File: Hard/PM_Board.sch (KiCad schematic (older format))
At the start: 66 parts, among them J1 Micro_SD_Card_Det_Hirose_DM3AT, J101 LiPo_V+, J102 LiPo_V-, J2 KRC_Conn_SWD, J3 USB_B_Micro, J4 KRC_Conn_CAN, J5 KRC_Conn_CAN, J6 Umbilical, Q1 SSM6J501NU, Q2 2n7002, U1 CY8C58xxLTI-LPxxx, U2 INA226, U3 NCV7342, Y1 24MHz

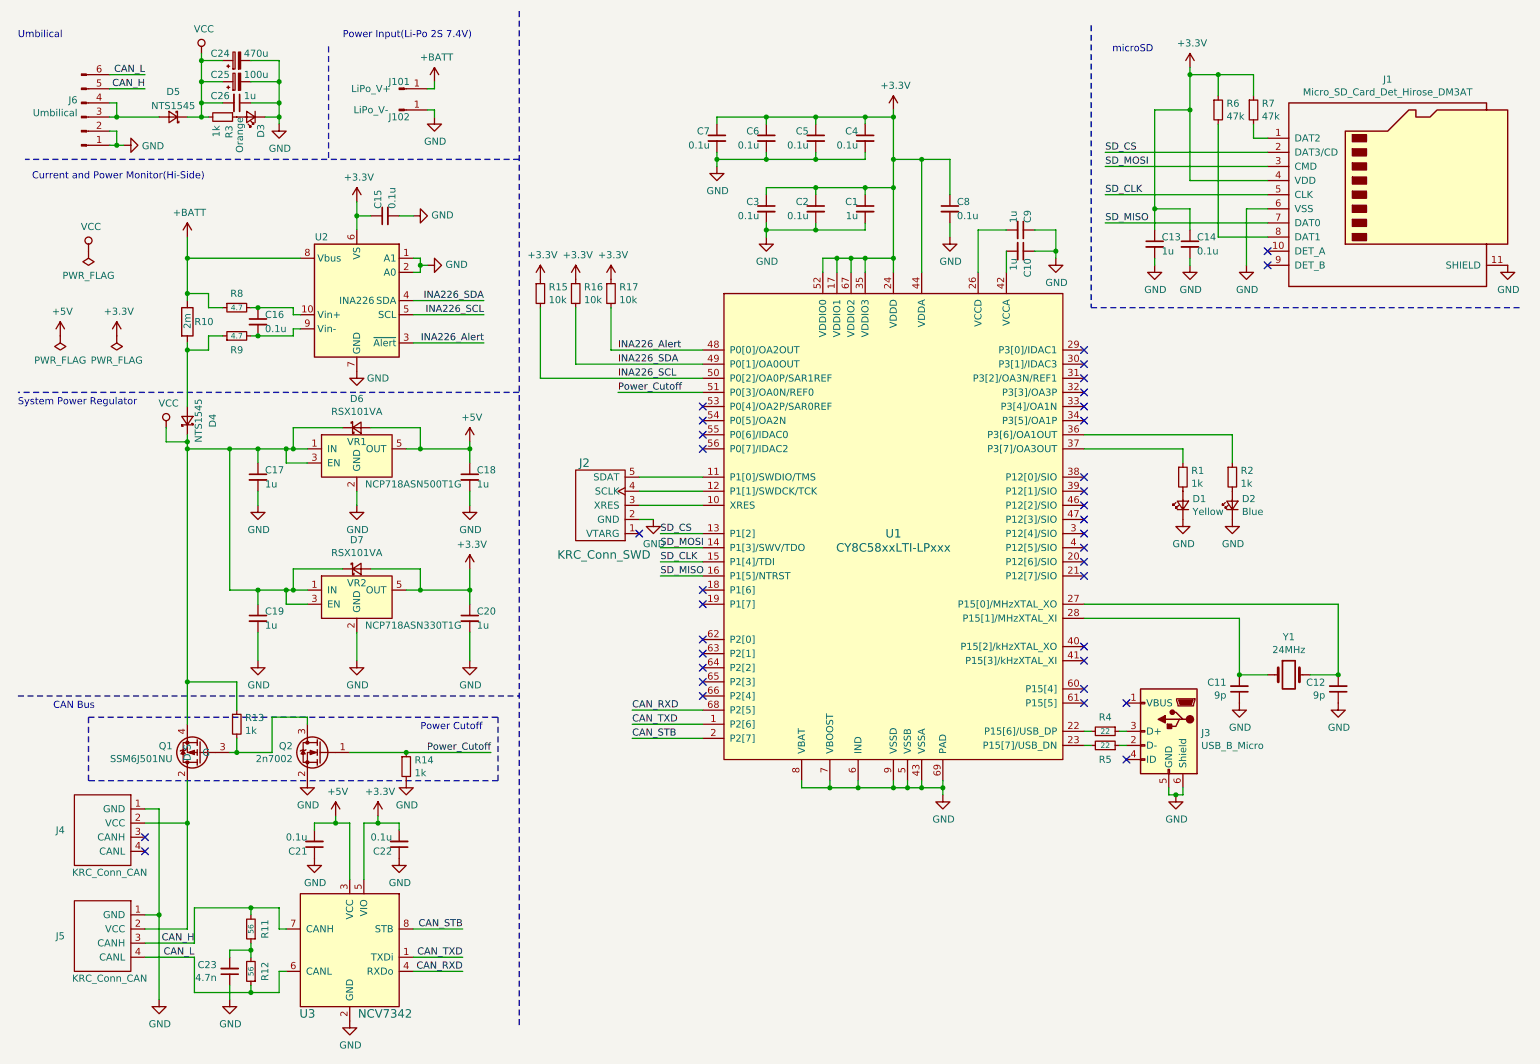
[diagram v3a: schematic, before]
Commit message: [update] SDカード用のLDOを追加
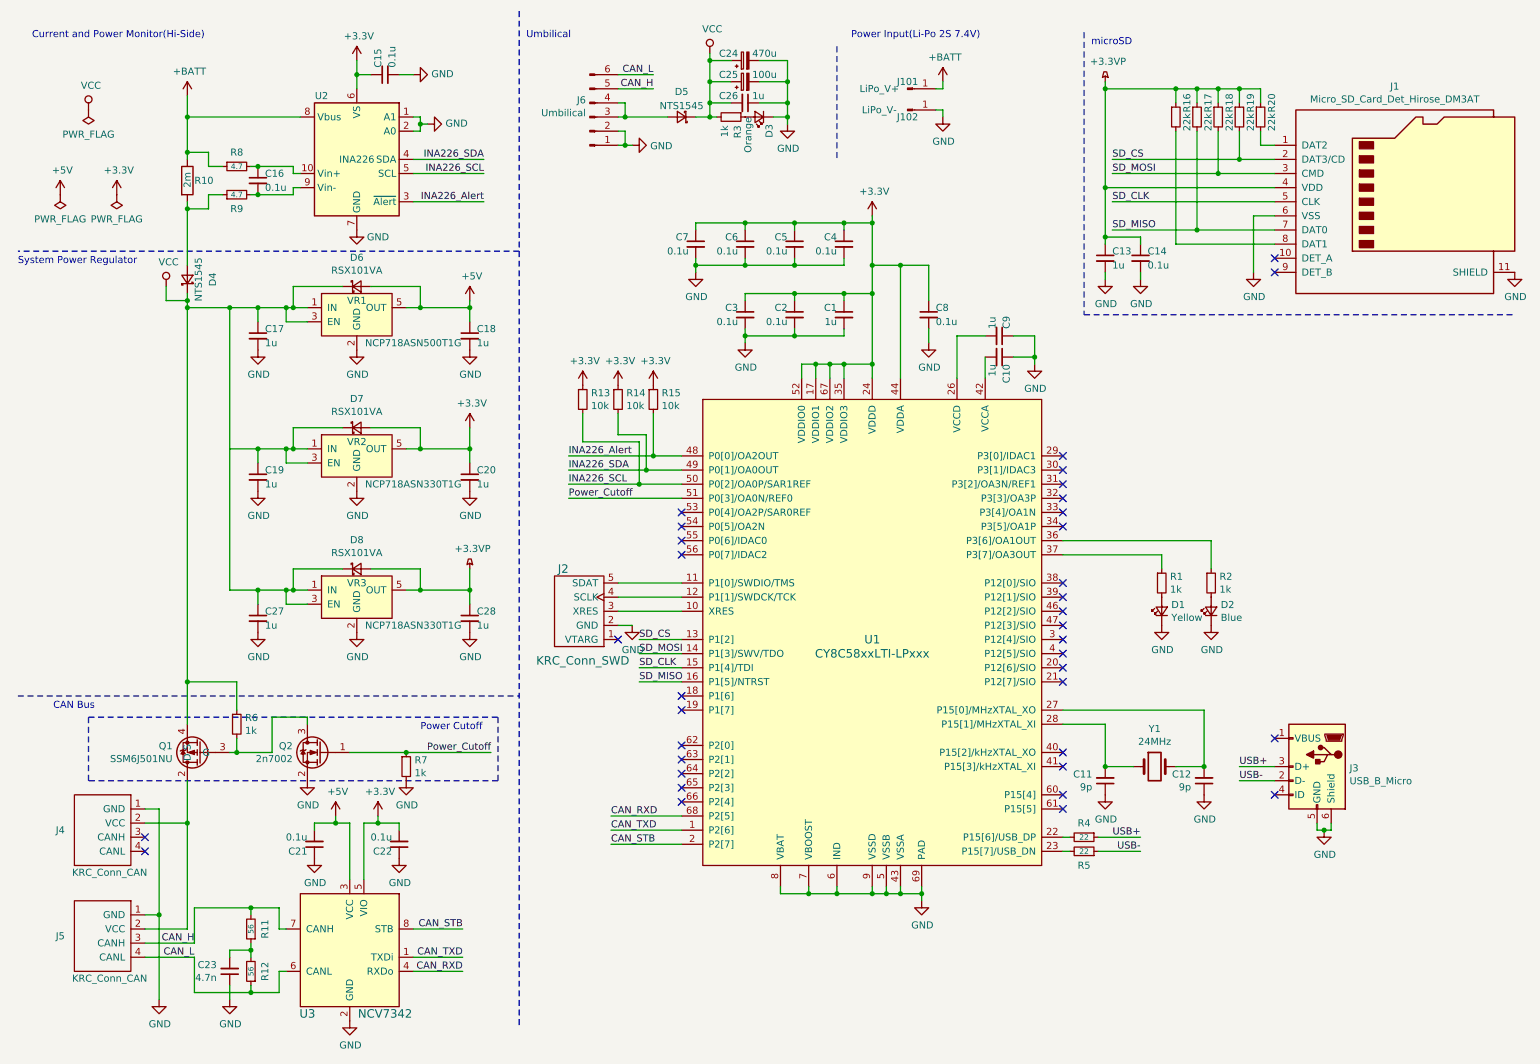
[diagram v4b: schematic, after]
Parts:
- removed R6, R7: 47k, Resistor_SMD:R_0402_1005Metric, symbol Device:R_Small
- added C27, C28: 1u, Capacitor_SMD:C_0402_1005Metric, symbol Device:C_Small
- added D8: RSX101VA, Diode_SMD:D_TUMD2, symbol Device:D_Schottky_Small
- added R16, R17, R18, R19, R20: 22k, Resistor_SMD:R_0402_1005Metric, symbol Device:R_Small
- added VR3: NCP718ASN330T1G, Package_TO_SOT_SMD:TSOT-23-5, symbol KUTKiCad_symbol:NCP718ASN330T1G
- renumbered R15 to R13, R16 to R14, R17 to R15, R13 to R6, R14 to R7
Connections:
- net +3V3: no longer C13.1, C14.1, J1.4 (VDD)
- net GND: now also C27.2, C28.2, VR3.2 (GND)
- net SD_CS: now also R19.2
- net SD_MISO: now also R17.2
- net SD_MOSI: now also R18.2
- net VCC: now also C27.1, D8.1 (K), VR3.1 (IN), VR3.3 (EN)
- net USB-: now reaches J3.2 (D-), R5.1
- net USB+: now reaches J3.3 (D+), R4.1
- net at J1.1 (DAT2): now also R20.2
- net at J1.8 (DAT1): now also R16.2
- new net +3.3VP: C13.1, C14.1, C28.1, D8.2 (A), J1.4 (VDD), R16.1, R17.1, R18.1, R19.1, R20.1, VR3.5 (OUT)
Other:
- moved on the sheet: C1, C10, C11, C12, C15, C16, C17, C18, C19, C2, C20, C24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

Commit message: [add] ダイオードの選定を変更。PchMOSFETの選定を変更。パターンを引き直し。ガーバ出力
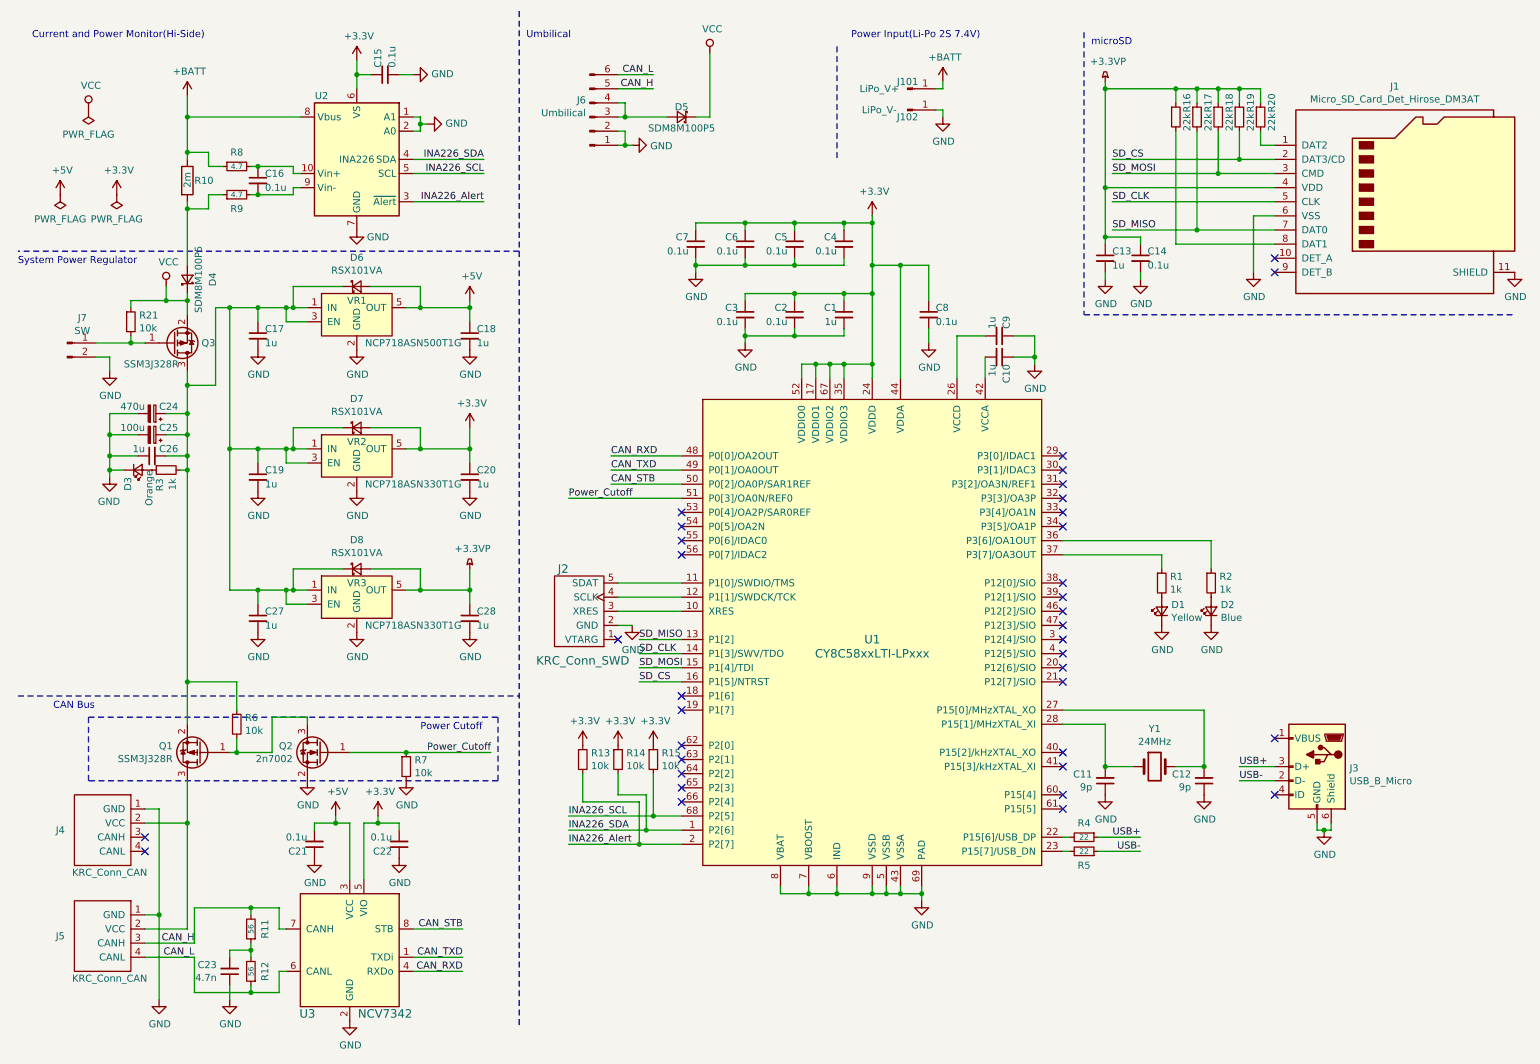
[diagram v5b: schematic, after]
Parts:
- removed Q1: SSM6J501NU, KUTKiCad_footprint:UDFN6B, symbol KUTKiCad_symbol:SSM6J501NU
- added J7: SW, KUTKiCad_footprint:Hirose_DF1E_DF1E-2P-2.5DS_1x02_P2.5mm_Vertical, symbol Connector:Conn_01x02_Male
- added Q1, Q3: SSM3J328R, Package_TO_SOT_SMD:SOT-23, symbol Device:Q_PMOS_GSD
- added R21: 10k, Resistor_SMD:R_0402_1005Metric, symbol Device:R_Small
- D4, D5: value NTS1545 -> SDM8M100P5; footprint KUTKiCad_footprint:DFN5_5x6_1.27P -> KUTKiCad_footprint:D_PowerDI5; Link https://www.digikey.jp/product-detail/ja/on-semiconductor/N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 -> https://www.digikey.jp/product-detail/ja/diodes-incorporate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; MPN NTS1545MFST1G -> SDM8M100P5-13
- R6, R7: value 1k -> 10k; Link https://www.digikey.jp/product-detail/ja/panasonic-electronic-components/ERJ-2GEJ102X/P1.0KJCT-ND/146897 -> https://www.digikey.jp/product-detail/ja/panasonic-electronic-components/ERJ-2GEJ103X/P10KJCT-ND/146734; MPN ERJ-2GEJ102X -> ERJ-2GEJ103X; Value 1kΩ -> 10kΩ
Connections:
- net CAN_RXD: now also U1.48 (P0[0]/OA2OUT); no longer U1.68 (P2[5])
- net CAN_STB: now also U1.50 (P0[2]/OA0P/SAR1REF); no longer U1.2 (P2[7])
- net CAN_TXD: now also U1.49 (P0[1]/OA0OUT); no longer U1.1 (P2[6])
- net GND: now also J7.2 (Pin_2)
- net INA226_Alert: now also R13.2, U1.2 (P2[7]); no longer R15.2, U1.48 (P0[0]/OA2OUT)
- net INA226_SCL: now also R15.2, U1.68 (P2[5]); no longer R13.2, U1.50 (P0[2]/OA0P/SAR1REF)
- net INA226_SDA: now also U1.1 (P2[6]); no longer U1.49 (P0[1]/OA0OUT)
- net SD_CLK: now also U1.14 (P1[3]/SWV/TDO); no longer U1.15 (P1[4]/TDI)
- net SD_CS: now also U1.16 (P1[5]/NTRST); no longer U1.13 (P1[2])
- net SD_MISO: now also U1.13 (P1[2]); no longer U1.16 (P1[5]/NTRST)
- net SD_MOSI: now also U1.15 (P1[4]/TDI); no longer U1.14 (P1[3]/SWV/TDO)
- net VCC: now also Q3.2 (S), R21.1; no longer C17.1, C19.1, C24.1, C25.1, C26.2, C27.1, D6.1 (K), D7.1 (K), D8.1 (K), R3.2, R6.1, VR1.1 (IN), VR1.3 (EN), VR2.1 (IN), VR2.3 (EN), VR3.1 (IN), VR3.3 (EN)
- net at J4.2 (VCC), J5.2 (VCC): now also Q1.3 (D)
- net at Q2.3 (D), R6.2: now also Q1.1 (G)
- new net: C17.1, C19.1, C24.1, C25.1, C26.2, C27.1, D6.1 (K), D7.1 (K), D8.1 (K), Q1.2 (S), Q3.3 (D), R3.2, R6.1, VR1.1 (IN), VR1.3 (EN), VR2.1 (IN), VR2.3 (EN), VR3.1 (IN), VR3.3 (EN)
- new net: J7.1 (Pin_1), Q3.1 (G), R21.2
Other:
- moved on the sheet: C24, C25, C26, D3, R13, R14, R15, R3

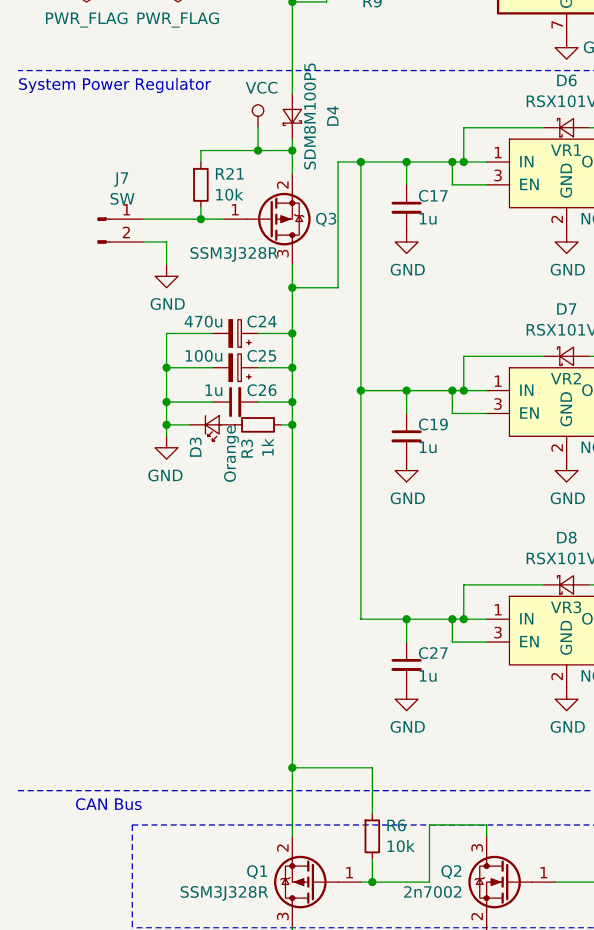
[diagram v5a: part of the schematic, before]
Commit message: [update] パスコンの位置を変更
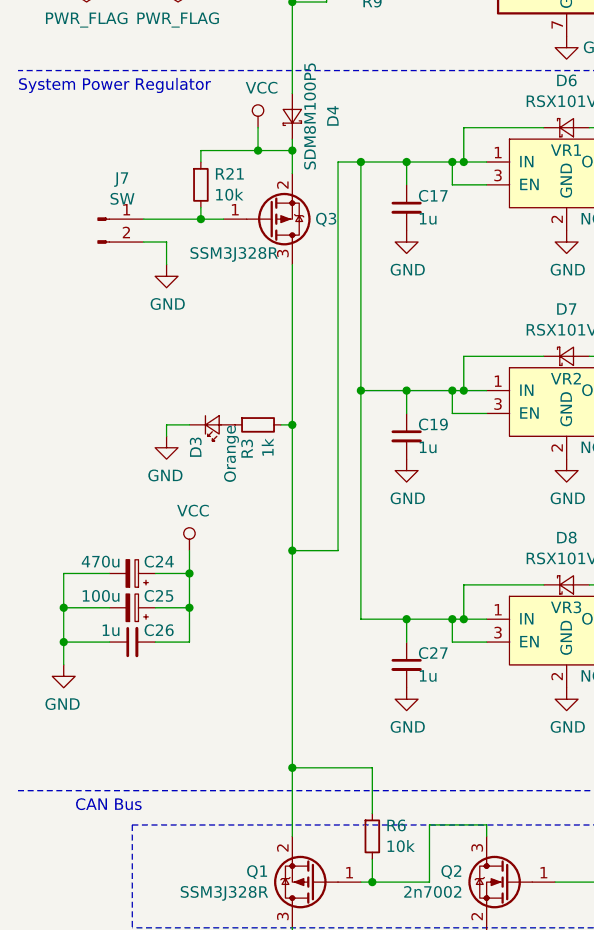
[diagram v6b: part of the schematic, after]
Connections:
- net VCC: now also C24.1, C25.1, C26.2
- net at C17.1, C19.1, C27.1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: no longer C24.1, C25.1, C26.2
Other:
- moved on the sheet: C24, C25, C26
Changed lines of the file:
@@
 L Device:CP_Small C24
 U 1 1 5DD1D31A
-P 1450 3250
-F 0 "C24" V 1500 3300 50  0000 L CNN
-F 1 "470u" V 1500 3200 50  0000 R CNN
-F 2 "Capacitor_SMD:CP_Elec_10x10" H 1450 3250 50  0001 C CNN
-F 3 "https://products.nichicon.co.jp/en/pdf/XJA043/e-uwt.pdf" H 1450 3250 50  0001 C CNN
-F 4 "Digikey" H 1450 3250 50  0001 C CNN "Agency"
-F 5 "UWT1E471MNL1GS" H 1450 3250 50  0001 C CNN "MPN"
-F 6 "https://www.digikey.jp/product-detail/ja/nichicon/UWT1E471MNL1GS/493-2194-1-ND/590169" H 1450 3250 50  0001 C CNN "Link"
-F 7 "470uF" H 1450 3250 50  0001 C CNN "Value"
-	1    1450 3250
+P 1000 4300
+F 0 "C24" V 1050 4350 50  0000 L CNN
+F 1 "470u" V 1050 4250 50  0000 R CNN
+F 2 "Capacitor_SMD:CP_Elec_10x10" H 1000 4300 50  0001 C CNN
+F 3 "https://products.nichicon.co.jp/en/pdf/XJA043/e-uwt.pdf" H 1000 4300 50  0001 C CNN
+F 4 "Digikey" H 1000 4300 50  0001 C CNN "Agency"
+F 5 "UWT1E471MNL1GS" H 1000 4300 50  0001 C CNN "MPN"
+F 6 "https://www.digikey.jp/product-detail/ja/nichicon/UWT1E471MNL1GS/493-2194-1-ND/590169" H 1000 4300 50  0001 C CNN "Link"
+F 7 "470uF" H 1000 4300 50  0001 C CNN "Value"
+	1    1000 4300
 	0    1    -1   0
 $EndComp
@@
 L Device:CP_Small C25
 U 1 1 5DD1D9F5
-P 1450 3400
-F 0 "C25" V 1500 3450 50  0000 L CNN
-F 1 "100u" V 1500 3350 50  0000 R CNN
-F 2 "Capacitor_SMD:CP_Elec_6.3x7.7" H 1450 3400 50  0001 C CNN
-F 3 "https://products.nichicon.co.jp/en/pdf/XJA043/e-uwt.pdf" H 1450 3400 50  0001 C CNN
-F 4 "Digikey" H 1450 3400 50  0001 C CNN "Agency"
-F 5 "UWT1E101MCL1GS" H 1450 3400 50  0001 C CNN "MPN"
-F 6 "https://www.digikey.jp/product-detail/ja/nichicon/UWT1E101MCL1GS/493-2190-1-ND/590165" H 1450 3400 50  0001 C CNN "Link"
-F 7 "100uF" H -250 2500 50  0001 C CNN "Value"
-	1    1450 3400
+P 1000 4450
+F 0 "C25" V 1050 4500 50  0000 L CNN
+F 1 "100u" V 1050 4400 50  0000 R CNN
+F 2 "Capacitor_SMD:CP_Elec_6.3x7.7" H 1000 4450 50  0001 C CNN
+F 3 "https://products.nichicon.co.jp/en/pdf/XJA043/e-uwt.pdf" H 1000 4450 50  0001 C CNN
+F 4 "Digikey" H 1000 4450 50  0001 C CNN "Agency"
+F 5 "UWT1E101MCL1GS" H 1000 4450 50  0001 C CNN "MPN"
+F 6 "https://www.digikey.jp/product-detail/ja/nichicon/UWT1E101MCL1GS/493-2190-1-ND/590165" H 1000 4450 50  0001 C CNN "Link"
+F 7 "100uF" H -700 3550 50  0001 C CNN "Value"
+	1    1000 4450
 	0    1    -1   0
 $EndComp
 Wire Wire Line
-	1700 3250 1550 3250
-Wire Wire Line
-	1550 3400 1700 3400
+	1250 4300 1100 4300
+Wire Wire Line
+	1100 4450 1250 4450
 $Comp
 L power:GND #PWR0146
@@
 $EndComp
 Wire Wire Line
-	1150 3400 1350 3400
-Wire Wire Line
-	1150 3250 1350 3250
+	700  4450 900  4450
+Wire Wire Line
+	700  4300 900  4300
 Wire Wire Line
 	1250 3650 1150 3650
-Connection ~ 1150 3650
 Wire Wire Line
 	1150 3650 1150 3700
@@
 	0    -1   1    0
 $EndComp
-Connection ~ 1150 3400
-Wire Wire Line
-	1150 3400 1150 3550
+Connection ~ 700  4450
+Wire Wire Line
+	700  4450 700  4600
 $Comp
 L Device:C_Small C26
 U 1 1 5DF210F4
-P 1450 3550
-F 0 "C26" V 1500 3500 50  0000 R CNN
-F 1 "1u" V 1500 3600 50  0000 L CNN
-F 2 "Capacitor_SMD:C_0402_1005Metric" H 1450 3550 50  0001 C CNN
-F 3 "https://search.murata.co.jp/Ceramy/image/img/A01X/G101/ENG/GRM155R61E105KA12-01.pdf" H 1450 3550 50  0001 C CNN
-F 4 "Digikey" H 1450 3550 50  0001 C CNN "Agency"
-F 5 "GRM155R61E105KA12D" H 1450 3550 50  0001 C CNN "MPN"
-F 6 "1uF" H 1450 3550 50  0001 C CNN "Value"
-F 7 "https://www.digikey.jp/product-detail/ja/murata-electronics/GRM155R61E105KA12D/490-10017-1-ND/5026367" H -250 2500 50  0001 C CNN "Link"
-	1    1450 3550
+P 1000 4600
+F 0 "C26" V 1050 4550 50  0000 R CNN
+F 1 "1u" V 1050 4650 50  0000 L CNN
+F 2 "Capacitor_SMD:C_0402_1005Metric" H 1000 4600 50  0001 C CNN
+F 3 "https://search.murata.co.jp/Ceramy/image/img/A01X/G101/ENG/GRM155R61E105KA12-01.pdf" H 1000 4600 50  0001 C CNN
+F 4 "Digikey" H 1000 4600 50  0001 C CNN "Agency"
+F 5 "GRM155R61E105KA12D" H 1000 4600 50  0001 C CNN "MPN"
+F 6 "1uF" H 1000 4600 50  0001 C CNN "Value"
+F 7 "https://www.digikey.jp/product-detail/ja/murata-electronics/GRM155R61E105KA12D/490-10017-1-ND/5026367" H -700 3550 50  0001 C CNN "Link"
+	1    1000 4600
 	0    -1   -1   0
 $EndComp
 Wire Wire Line
-	1150 3250 1150 3400
-Wire Wire Line
-	1550 3550 1700 3550
-Wire Wire Line
-	1350 3550 1150 3550
-Connection ~ 1150 3550
-Wire Wire Line
-	1150 3550 1150 3650
+	700  4300 700  4450
+Wire Wire Line
+	1100 4600 1250 4600
+Wire Wire Line
+	900  4600 700  4600
 $Comp
 L power:VCC #PWR0147
@@
 $EndComp
 Wire Wire Line
-	1900 2500 1900 3050
-Wire Wire Line
-	1700 3050 1700 3250
-Wire Wire Line
-	1700 2950 1700 3050
-Connection ~ 1700 3050
-Wire Wire Line
-	1900 3050 1700 3050
-Wire Wire Line
 	1550 2450 1300 2450
 Wire Wire Line
@@
 Wire Wire Line
 	5400 700  5400 1150
-Connection ~ 1700 3250
-Wire Wire Line
-	1700 3250 1700 3400
-Connection ~ 1700 3400
-Wire Wire Line
-	1700 3400 1700 3550
-Connection ~ 1700 3550
-Wire Wire Line
-	1700 3550 1700 3650
 Wire Wire Line
 	1650 3650 1700 3650
+Wire Wire Line
+	1900 2500 1900 4200
+Wire Wire Line
+	1700 4200 1700 5150
+Wire Wire Line
+	1900 4200 1700 4200
+Wire Wire Line
+	1700 2950 1700 3650
+Connection ~ 1700 4200
 Connection ~ 1700 3650
 Wire Wire Line
-	1700 3650 1700 5150
+	1700 3650 1700 4200
+$Comp
+L power:VCC #PWR?
+U 1 1 5DBF619F
+P 1250 4200
+F 0 "#PWR?" H 1250 4050 50  0001 C CNN
+F 1 "VCC" H 1267 4373 50  0000 C CNN
+F 2 "" H 1250 4200 50  0001 C CNN
+F 3 "" H 1250 4200 50  0001 C CNN
+	1    1250 4200
+	1    0    0    -1
+$EndComp
+Wire Wire Line
+	1250 4200 1250 4300
+Wire Wire Line
+	1250 4300 1250 4450
+Connection ~ 1250 4300
+Wire Wire Line
+	1250 4450 1250 4600
+Connection ~ 1250 4450
+$Comp
+L power:GND #PWR?
+U 1 1 5DCA69C1
+P 700 4700
+F 0 "#PWR?" H 700 4450 50  0001 C CNN
+F 1 "GND" H 705 4527 50  0000 C CNN
+F 2 "" H 700 4700 50  0001 C CNN
+F 3 "" H 700 4700 50  0001 C CNN
+	1    700  4700
+	-1   0    0    -1
+$EndComp
+Wire Wire Line
+	700  4700 700  4600
+Connection ~ 700  4600
 $EndSCHEMATC
